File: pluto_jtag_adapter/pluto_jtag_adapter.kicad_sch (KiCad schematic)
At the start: 24 parts, among them J1 JTAG_UART_PLUTO, J2 Conn_01x08, J3 Conn_01x04, J4 USB_B_Micro, U1 FT2232HL, U2 AP2112K-3.3, U3 AP2112K-1.8

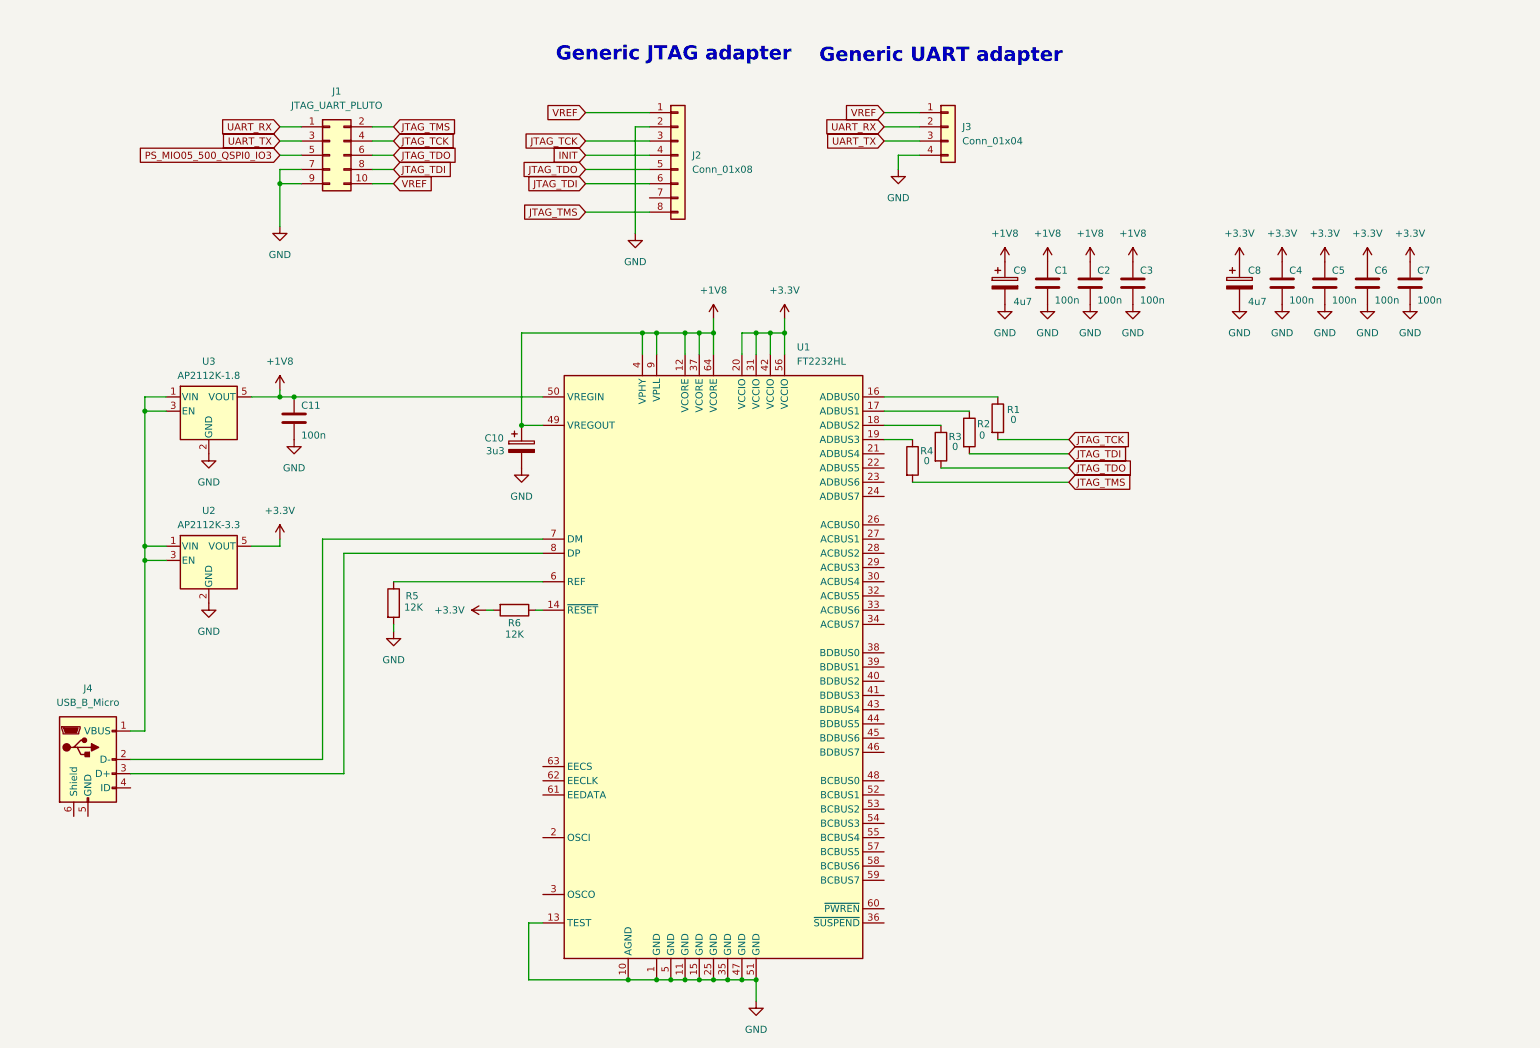
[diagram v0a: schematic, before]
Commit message: Add EEPROM and level shifters for ft2232hl chip
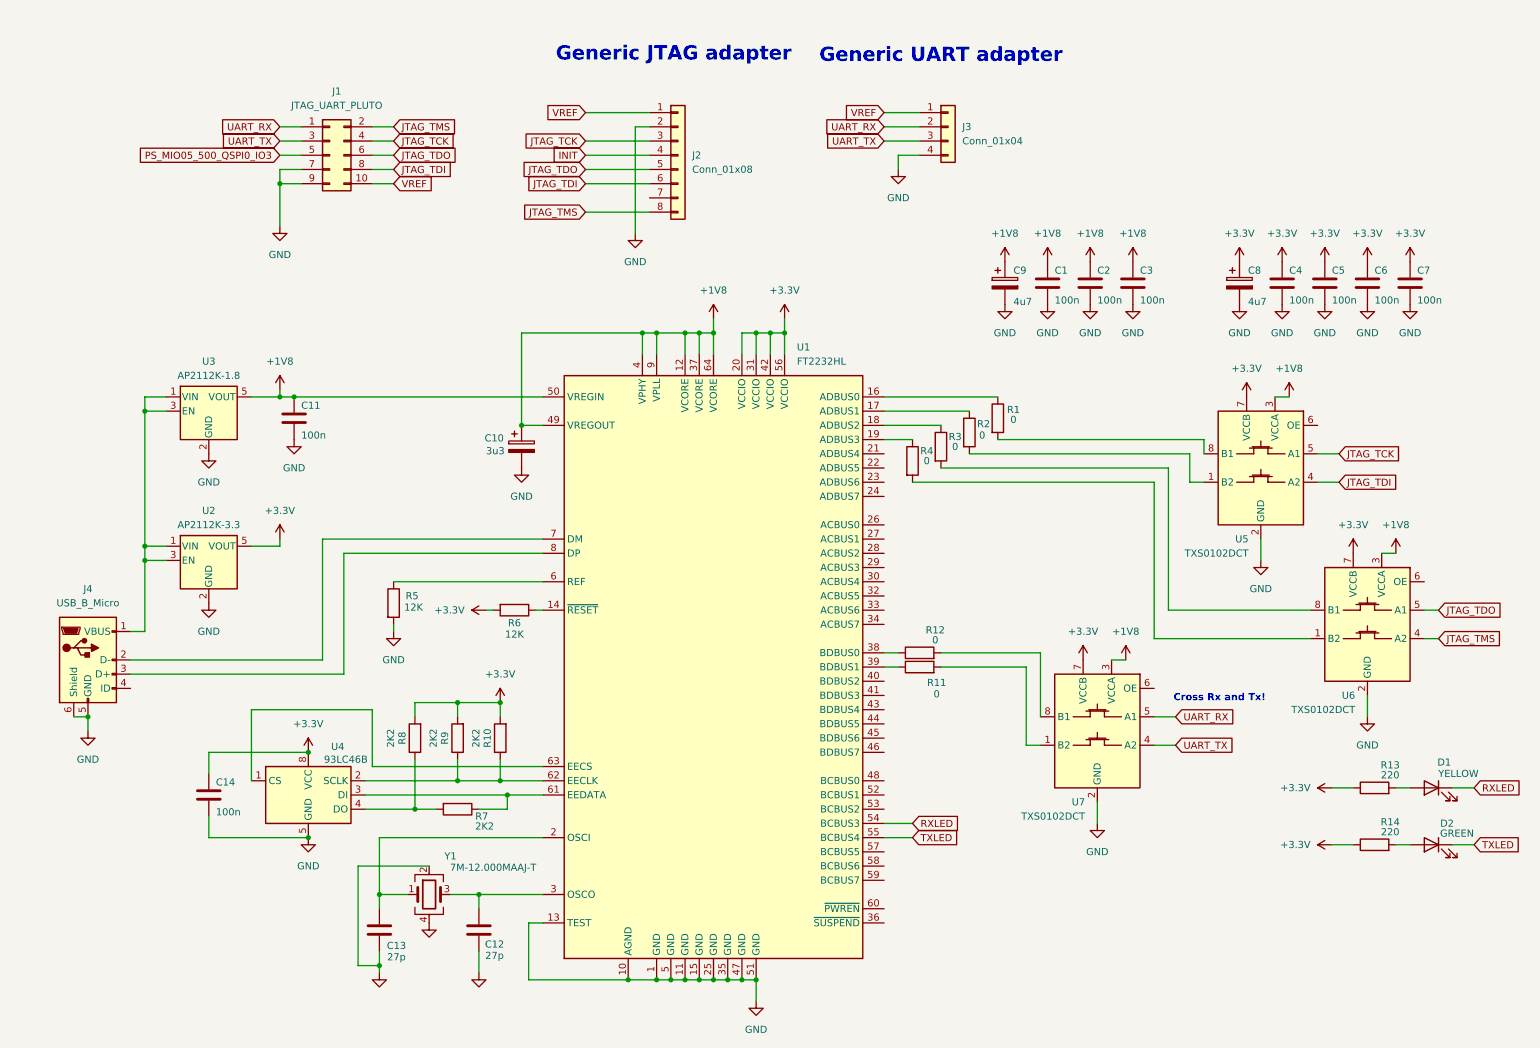
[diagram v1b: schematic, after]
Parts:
- added C12, C13: 27p, symbol Device:C
- added C14: 100n, symbol Device:C
- added D1: YELLOW, symbol Device:LED
- added D2: GREEN, symbol Device:LED
- added R10, R7, R8, R9: 2K2, Resistor_SMD:R_0603_1608Metric_Pad0.98x0.95mm_HandSolder, symbol Device:R
- added R11, R12: 0, Resistor_SMD:R_0603_1608Metric_Pad0.98x0.95mm_HandSolder, symbol Device:R
- added R13, R14: 220, Resistor_SMD:R_0603_1608Metric_Pad0.98x0.95mm_HandSolder, symbol Device:R
- added U4: 93LC46B, symbol Memory_EEPROM:93LCxxB
- added U5, U6, U7: TXS0102DCT, Package_SO:SSOP-8_2.95x2.8mm_P0.65mm, symbol Logic_LevelTranslator:TXS0102DCT
- added Y1: 7M-12.000MAAJ-T, symbol Device:Crystal_GND24
- R1, R2, R3, R4, R5, R6: footprint (none) -> Resistor_SMD:R_0603_1608Metric_Pad0.98x0.95mm_HandSolder
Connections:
- net +1V8: now also U5.3 (VCCA), U6.3 (VCCA), U7.3 (VCCA)
- net +3.3V: now also C14.1, R10.2, R13.1, R14.1, R8.2, R9.2, U4.8 (VCC), U5.7 (VCCB), U6.7 (VCCB), U7.7 (VCCB)
- net GND: now also J4.5 (GND), J4.6 (Shield), C12.1, C13.1, C14.2, U4.5 (GND), U5.2 (GND), U6.2 (GND), U7.2 (GND), Y1.2, Y1.4
- net JTAG_TCK: now also U5.5 (A1); no longer R1.2
- net JTAG_TDI: now also U5.4 (A2); no longer R2.2
- net JTAG_TDO: now also U6.5 (A1); no longer R3.2
- net JTAG_TMS: now also U6.4 (A2); no longer R4.2
- net UART_RX: now also U7.5 (A1)
- net UART_TX: now also U7.4 (A2)
- net at U1.2 (OSCI): now also C13.2, Y1.1
- net at U1.3 (OSCO): now also C12.2, Y1.3
- net at U1.38 (BDBUS0): now also R12.1
- net at U1.39 (BDBUS1): now also R11.1
- net RXLED: now reaches U1.54 (BCBUS3)
- net RXLED: now also D1.1 (K)
- net TXLED: now reaches U1.55 (BCBUS4)
- net TXLED: now also D2.1 (K)
- net at U1.61 (EEDATA): now also R7.1, U4.3 (DI)
- net at U1.62 (EECLK): now also R10.1, R9.1, U4.2 (SCLK)
- net at U1.63 (EECS): now also U4.1 (CS)
- new net: R4.2, U6.1 (B2)
- new net: R3.2, U6.8 (B1)
- new net: D1.2 (A), R13.2
- new net: R11.2, U7.1 (B2)
- new net: R7.2, R8.1, U4.4 (DO)
- new net: D2.2 (A), R14.2
- new net: R12.2, U7.8 (B1)
- new net: R2.2, U5.1 (B2)
- new net: R1.2, U5.8 (B1)
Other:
- note added: "Cross Rx and Tx!"
- moved on the sheet: J4

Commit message: Assign footprints to components. Wire up OE on level shifters
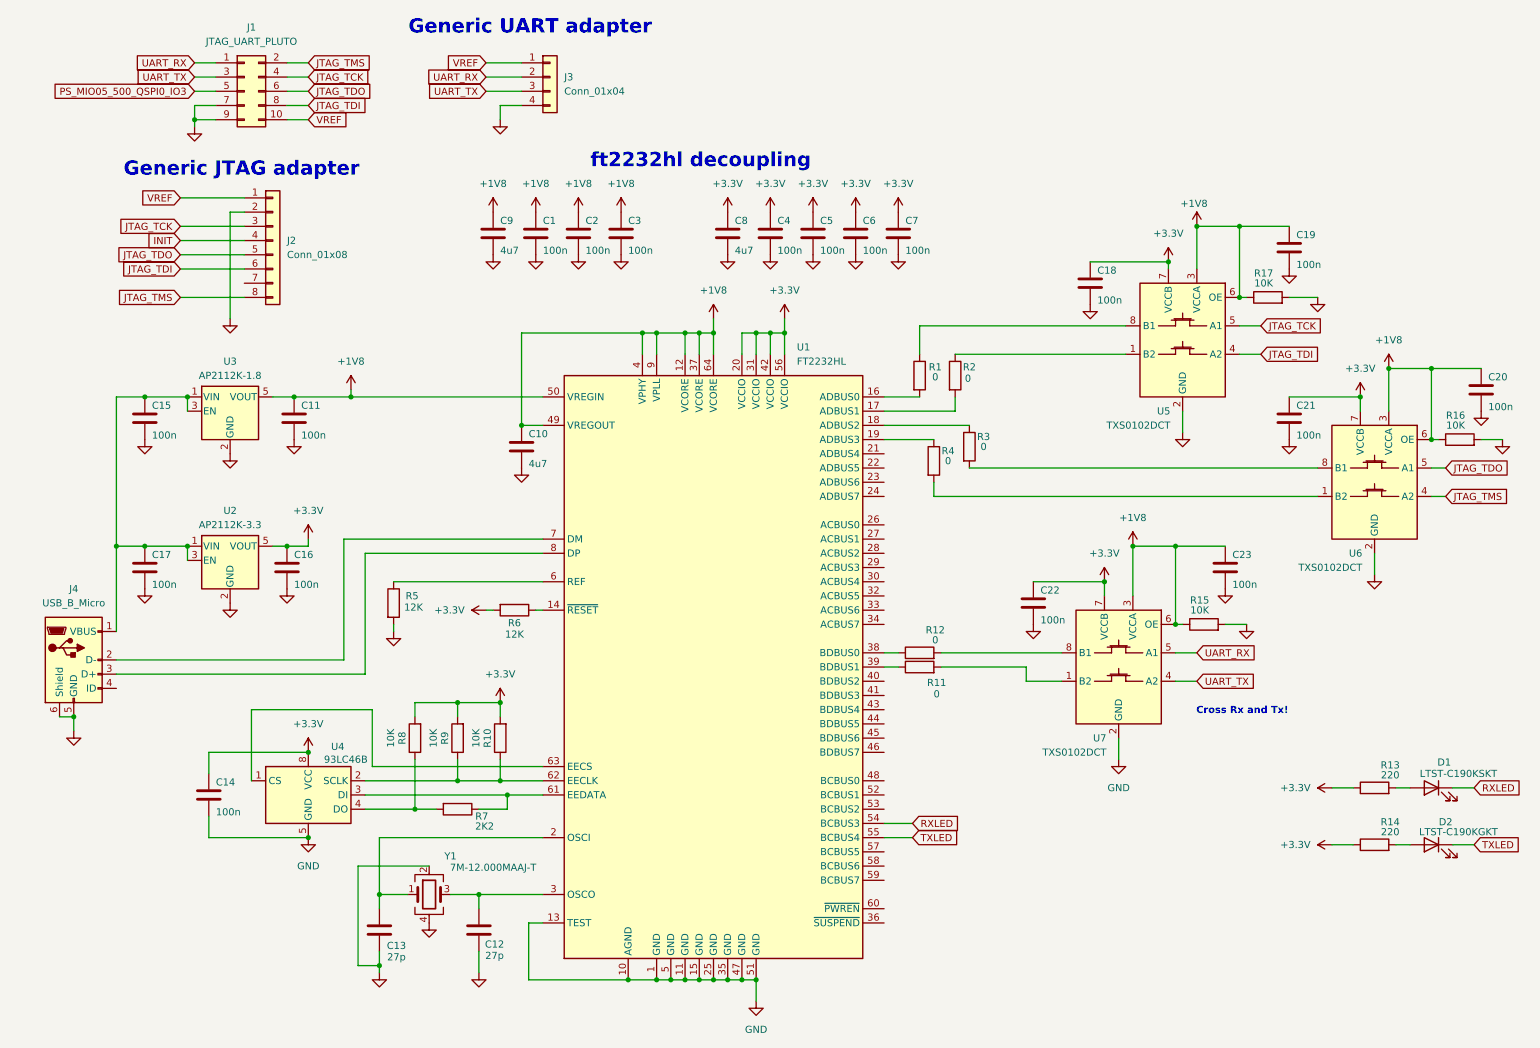
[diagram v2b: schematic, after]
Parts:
- removed C10: 3u3, symbol Device:C_Polarized
- removed C8, C9: 4u7, symbol Device:C_Polarized
- added C10, C8, C9: 4u7, Capacitor_SMD:C_0603_1608Metric_Pad1.08x0.95mm_HandSolder, symbol Device:C
- added C15, C16, C17, C18, C19, C20, C21, C22, C23: 100n, Capacitor_SMD:C_0603_1608Metric_Pad1.08x0.95mm_HandSolder, symbol Device:C
- added R15, R16, R17: 10K, Resistor_SMD:R_0603_1608Metric_Pad0.98x0.95mm_HandSolder, symbol Device:R
- C1, C11, C12, C13, C14, C2, C3, C4, C5, C6, C7: footprint (none) -> Capacitor_SMD:C_0603_1608Metric_Pad1.08x0.95mm_HandSolder
- D1: value YELLOW -> LTST-C190KSKT; footprint (none) -> LED_SMD:LED_0603_1608Metric
- D2: value GREEN -> LTST-C190KGKT; footprint (none) -> LED_SMD:LED_0603_1608Metric
- R10, R8, R9: value 2K2 -> 10K
- U4: footprint (none) -> Package_SO:SOIC-8_3.9x4.9mm_P1.27mm
- Y1: footprint (none) -> Crystal:Crystal_SMD_3225-4Pin_3.2x2.5mm_HandSoldering
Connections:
- net +1V8: now also U5.6 (OE), U6.6 (OE), U7.6 (OE), C10.1, C19.1, C20.1, C23.1, C9.1, R15.1, R16.1, R17.1
- net +3.3V: now also C16.1, C18.1, C21.1, C22.1, C8.1
- net GND: now also C10.2, C15.2, C16.2, C17.2, C18.2, C19.2, C20.2, C21.2, C22.2, C23.2, C8.2, C9.2, R15.2, R16.2, R17.2
- net at J4.1 (VBUS), U2.1 (VIN), U2.3 (EN)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: now also C15.1, C17.1
- net at U1.16 (ADBUS0): now also R1.2; no longer R1.1
- net at U1.17 (ADBUS1): now also R2.2; no longer R2.1
- net at U5.1 (B2): now also R2.1; no longer R2.2
- net at U5.8 (B1): now also R1.1; no longer R1.2
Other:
- note added: "ft2232hl decoupling"
- moved on the sheet: C1, C2, C3, C4, C5, C6, C7, J1, J2, J3, J4, R1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

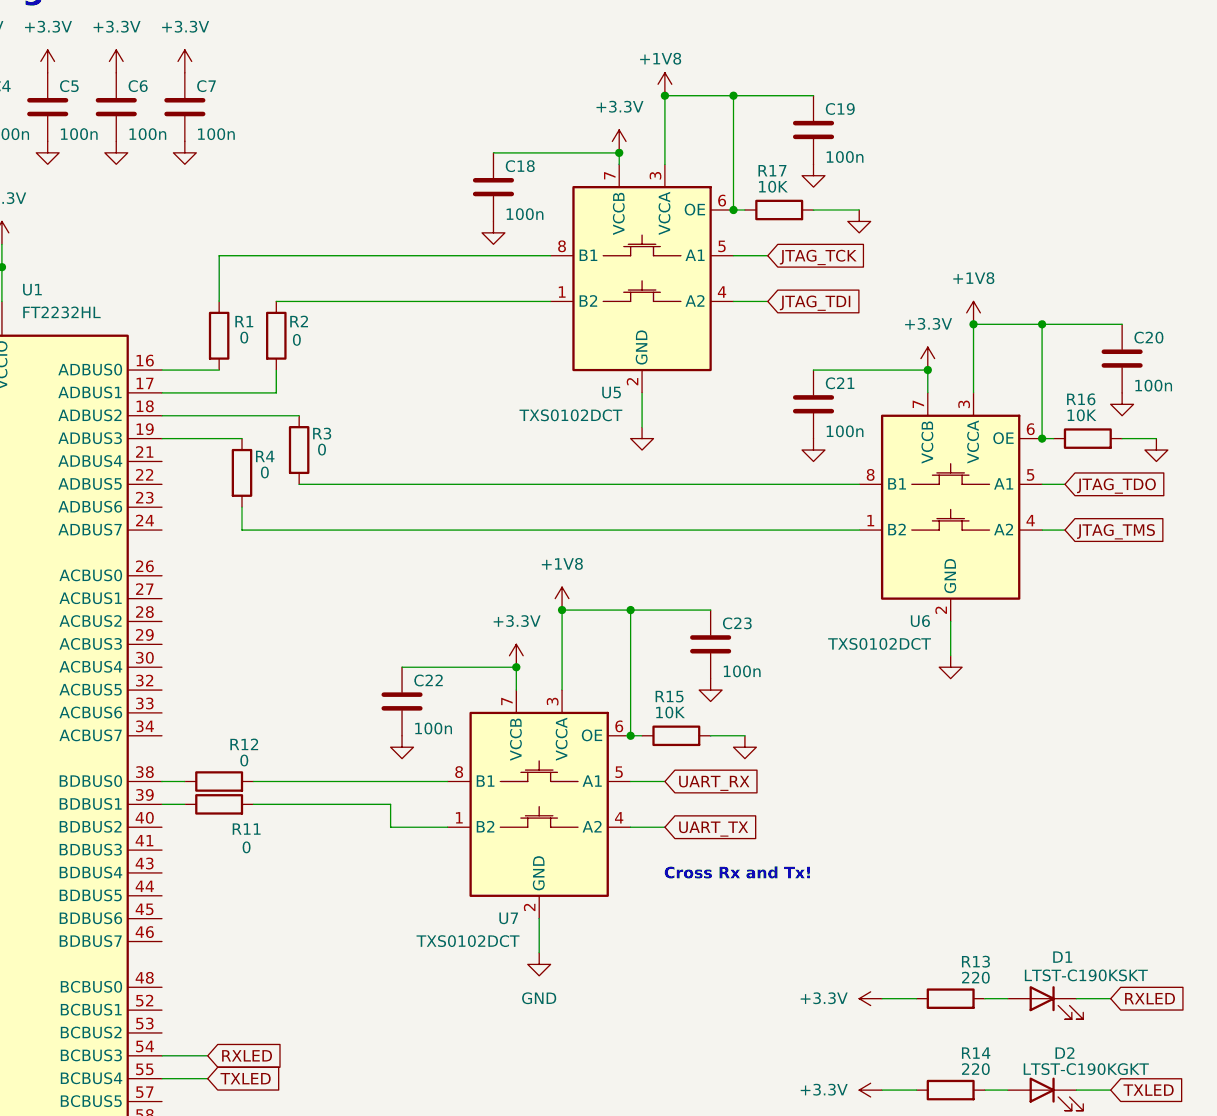
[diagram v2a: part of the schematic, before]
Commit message: Replace TXS level shifters with TXB (push-pull better for my application)
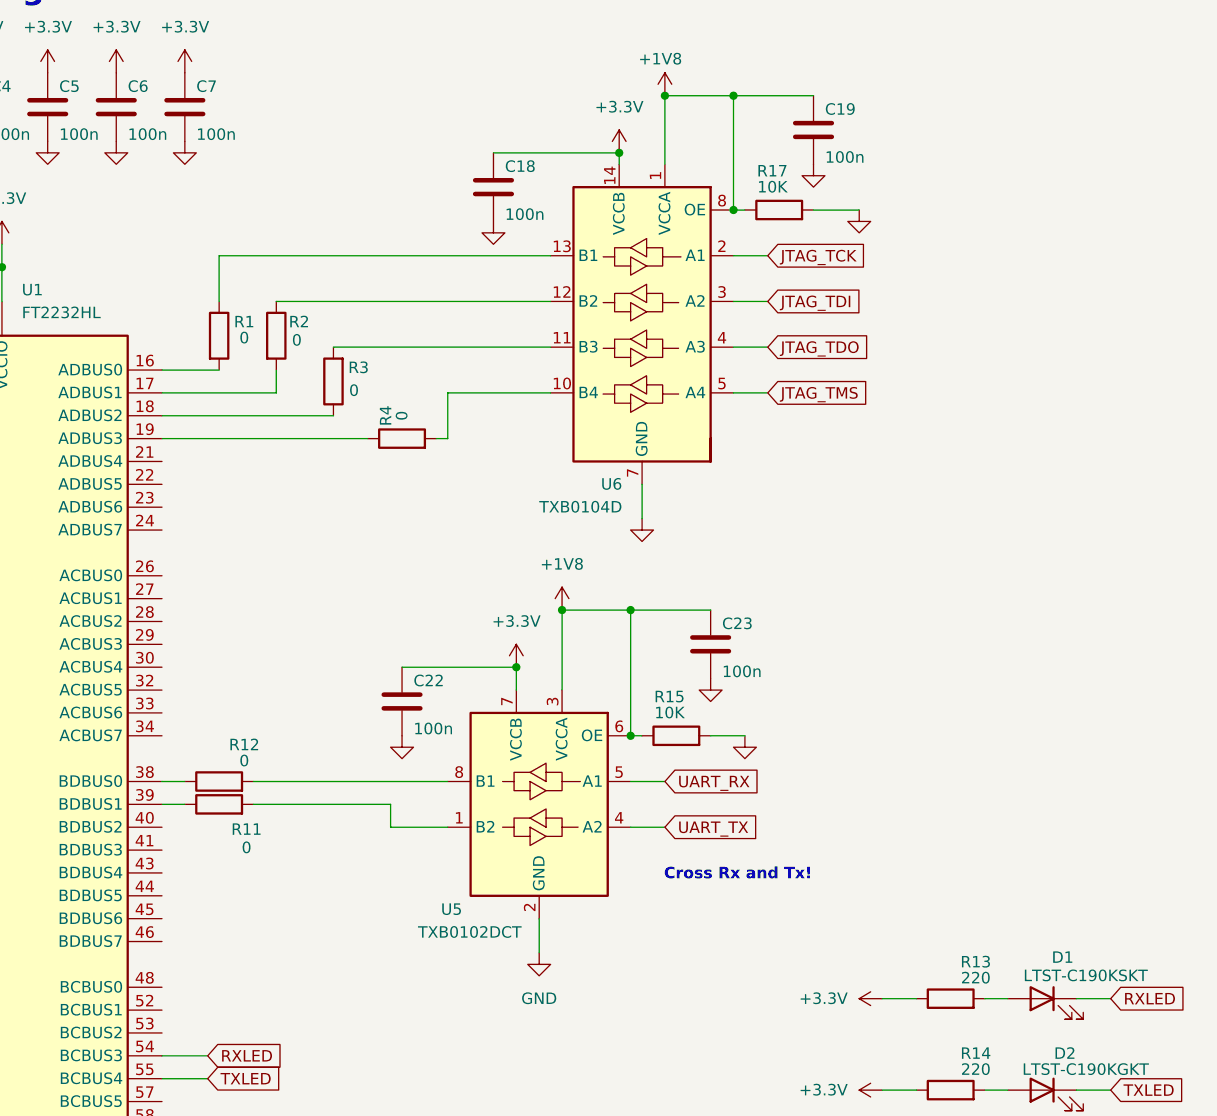
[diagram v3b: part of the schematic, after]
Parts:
- removed C20, C21: 100n, Capacitor_SMD:C_0603_1608Metric_Pad1.08x0.95mm_HandSolder, symbol Device:C
- removed R16: 10K, Resistor_SMD:R_0603_1608Metric_Pad0.98x0.95mm_HandSolder, symbol Device:R
- removed U5, U6, U7: TXS0102DCT, Package_SO:SSOP-8_2.95x2.8mm_P0.65mm, symbol Logic_LevelTranslator:TXS0102DCT
- added U5: TXB0102DCT, Package_SO:TSSOP-8_3x3mm_P0.65mm, symbol Logic_LevelTranslator:TXB0102DCT
- added U6: TXB0104D, Package_SO:SOIC-14_3.9x8.7mm_P1.27mm, symbol Logic_LevelTranslator:TXB0104D
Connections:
- net +1V8: now also U5.3 (VCCA), U5.6 (OE), U6.1 (VCCA), U6.8 (OE)
- net +3.3V: now also U5.7 (VCCB), U6.14 (VCCB)
- net GND: now also U5.2 (GND), U6.7 (GND)
- net JTAG_TCK: now also U6.2 (A1)
- net JTAG_TDI: now also U6.3 (A2)
- net JTAG_TDO: now also U6.4 (A3)
- net JTAG_TMS: now also U6.5 (A4)
- net UART_RX: now also U5.5 (A1)
- net UART_TX: now also U5.4 (A2)
- net at R4.2: now also U6.10 (B4)
- net at R3.2: now also U6.11 (B3)
- net at R11.2: now also U5.1 (B2)
- net at R12.2: now also U5.8 (B1)
- net at R2.1: now also U6.12 (B2)
- net at R1.1: now also U6.13 (B1)
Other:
- moved on the sheet: R3, R4
